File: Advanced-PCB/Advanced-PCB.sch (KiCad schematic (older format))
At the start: 150 parts, among them J1 USB_mini_micro_B, SW1 Esc, SW10 9, SW11 0, SW12 -, SW13 =, SW14 Back, SW15 `, SW2 1, SW3 2, SW4 3, SW5 4, SW6 5, SW7 6, SW8 7, SW9 8, U1 ATMEGA32U4, X1 16MHz

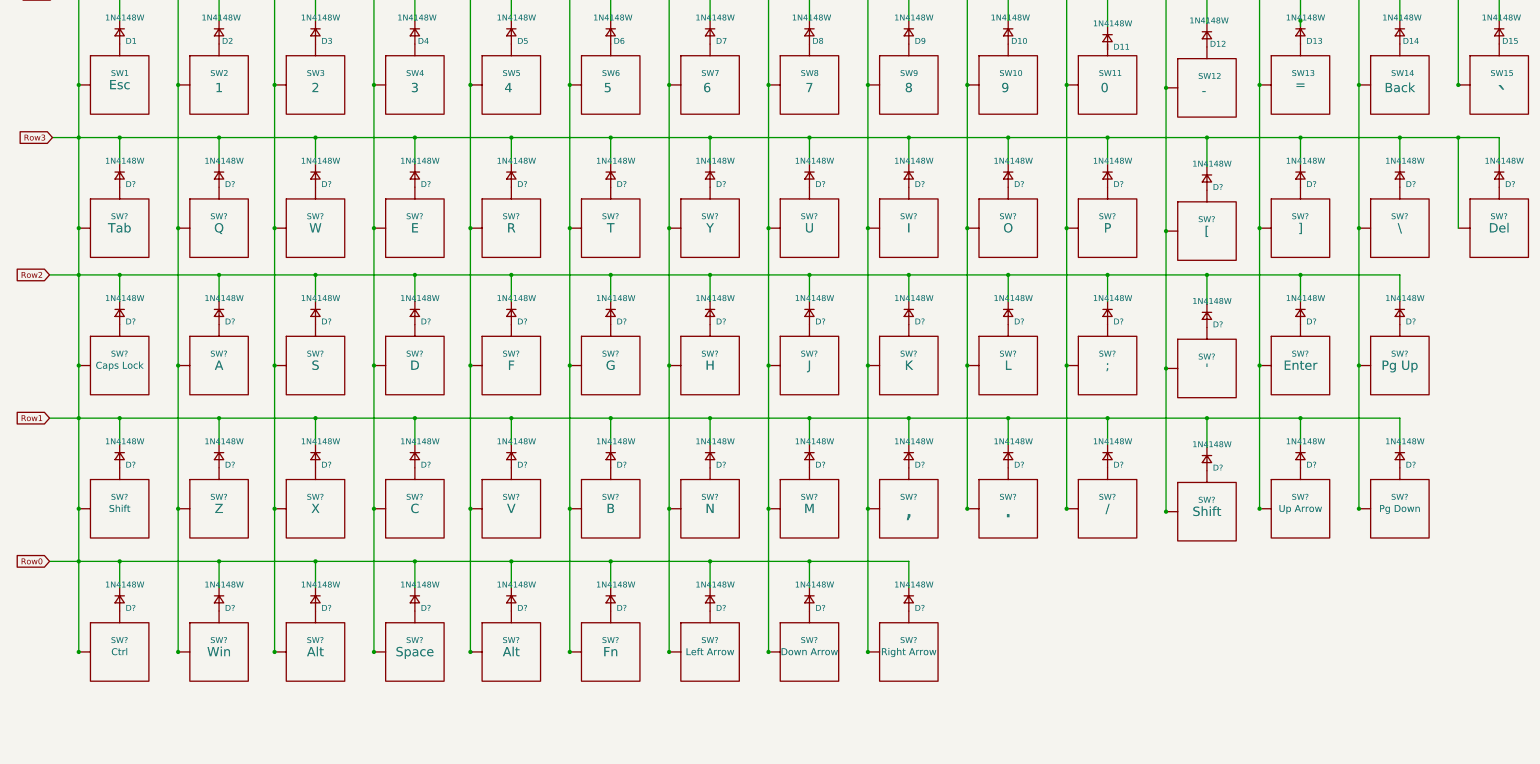
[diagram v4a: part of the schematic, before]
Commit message: Bottom Row Re-Alligned
Bottom Row Realigned to help with Trace in later steps.
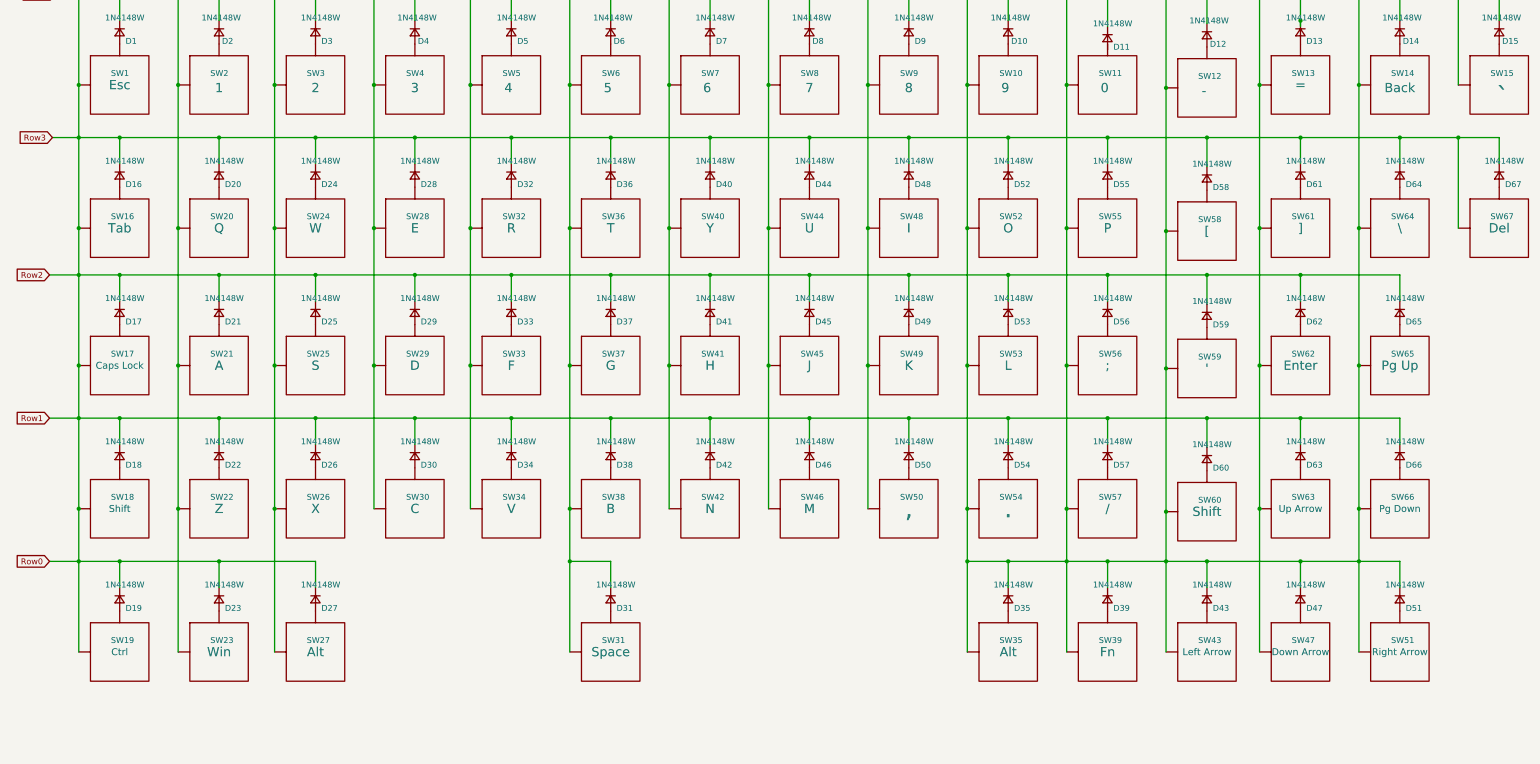
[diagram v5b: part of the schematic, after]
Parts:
- gave numbers to parts that had none: 104
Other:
- moved on the sheet: D31, D35, D39, D43, D47, D51, SW31, SW35, SW39, SW43, SW47, SW51

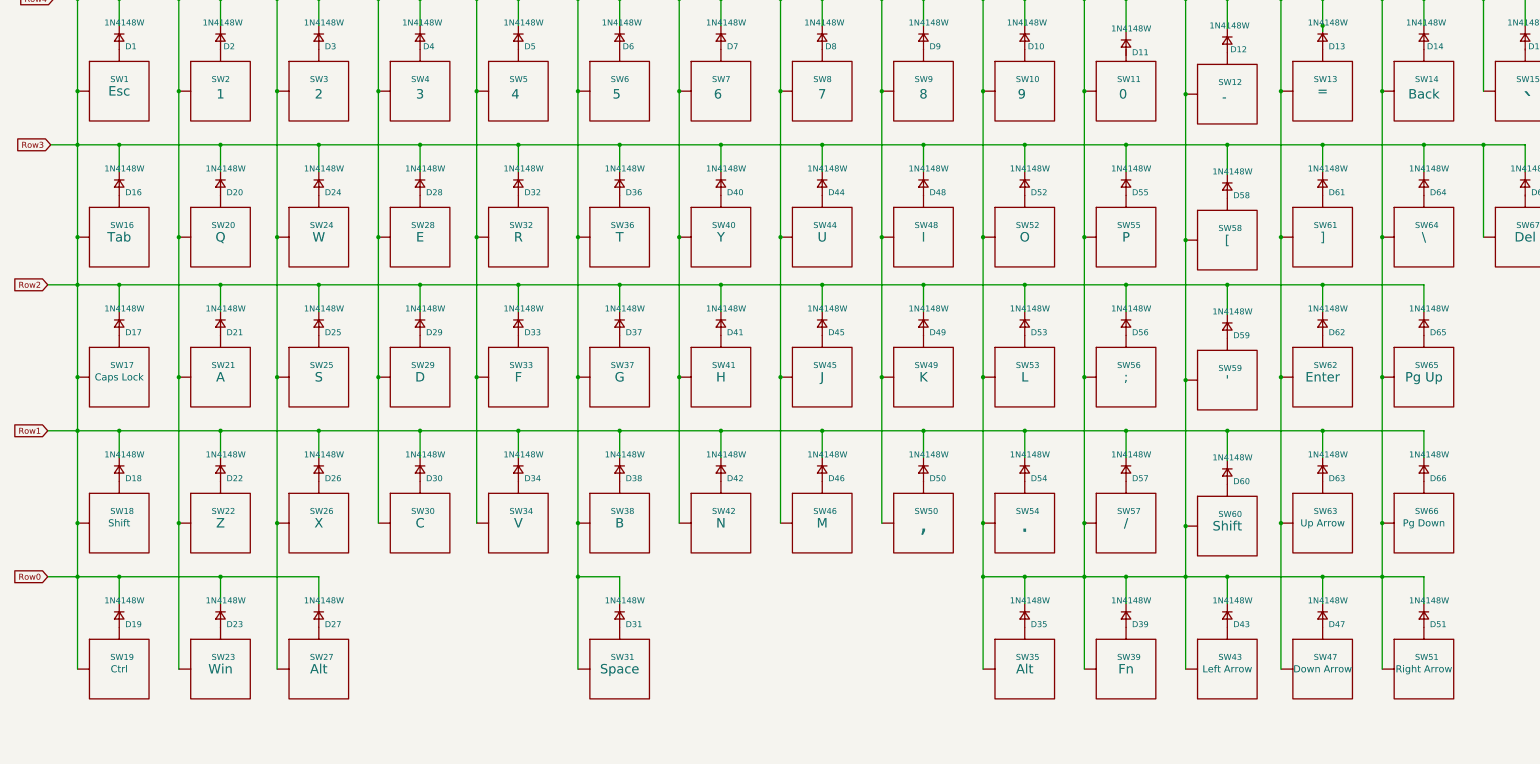
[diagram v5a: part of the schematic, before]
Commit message: KB Sizes Added
Non 1u switches sizes added to label.
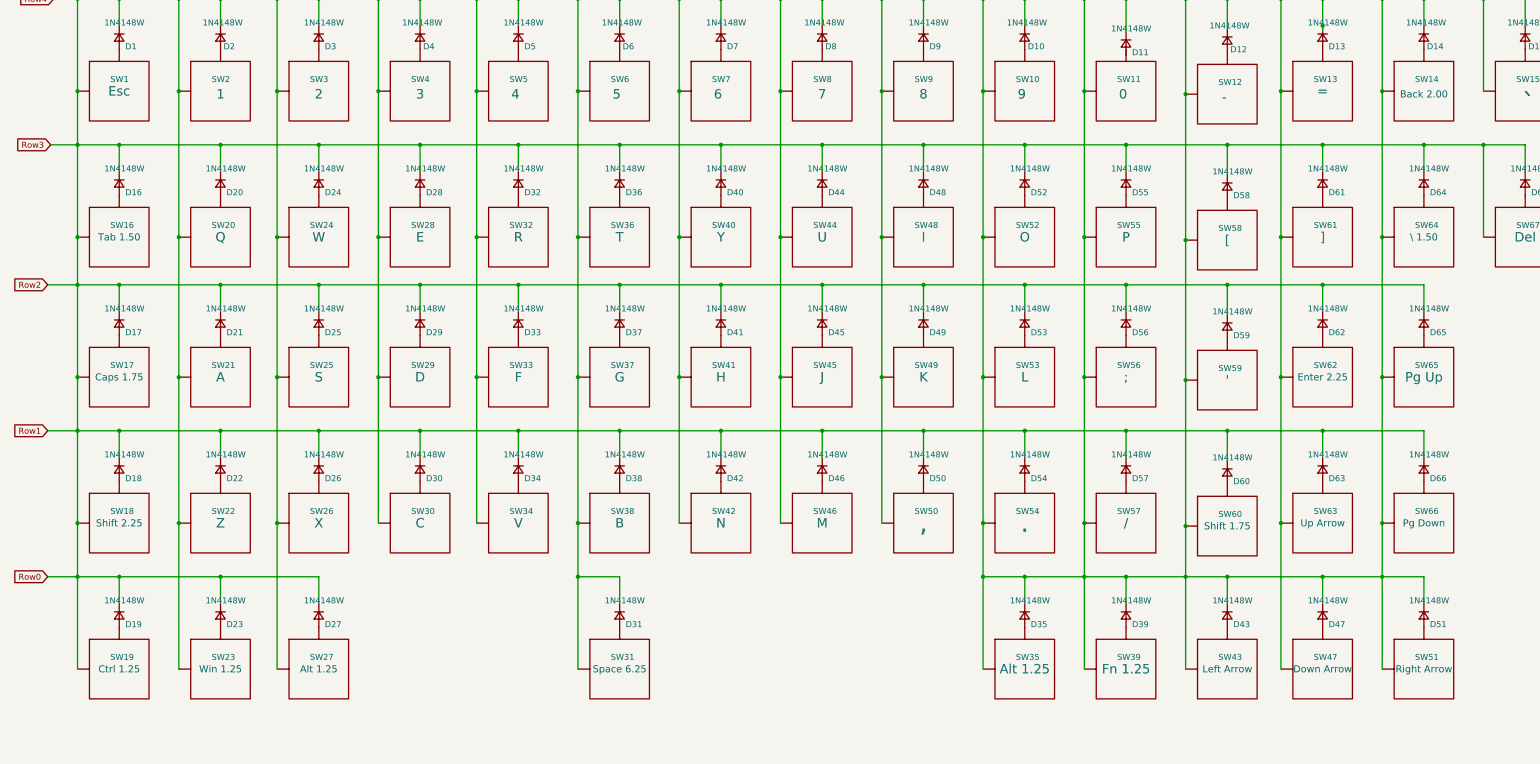
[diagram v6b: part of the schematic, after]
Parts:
- SW14: value Back -> Back 2.00
- SW16: value Tab -> Tab 1.50
- SW17: value Caps Lock -> Caps 1.75
- SW18: value Shift -> Shift 2.25
- SW19: value Ctrl -> Ctrl 1.25
- SW23: value Win -> Win 1.25
- SW27, SW35: value Alt -> Alt 1.25
- SW31: value Space -> Space 6.25
- SW39: value Fn -> Fn 1.25
- SW60: value Shift -> Shift 1.75
- SW62: value Enter -> Enter 2.25
- SW64: value \\ -> \\ 1.50
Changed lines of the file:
@@
 P 12550 1775
 F 0 "SW14" H 12475 1875 50  0000 L CNN
-F 1 "Back" H 12550 1750 79  0000 C CNN
+F 1 "Back 2.00" H 12550 1750 59  0000 C CNN
 F 2 "acheron_MXH:MX100H" H 12550 1775 50  0001 C CNN
 F 3 "" H 12550 1775 50  0001 C CNN
@@
 P 1600 3000
 F 0 "SW16" H 1525 3100 50  0000 L CNN
-F 1 "Tab" H 1600 3000 79  0000 C CNN
+F 1 "Tab 1.50" H 1600 3000 59  0000 C CNN
 F 2 "acheron_MXH:MX100H" H 1600 3000 50  0001 C CNN
 F 3 "" H 1600 3000 50  0001 C CNN
@@
 P 12550 3000
 F 0 "SW64" H 12475 3100 50  0000 L CNN
-F 1 "\\" H 12550 3000 79  0000 C CNN
+F 1 "\\ 1.50" H 12550 3000 59  0000 C CNN
 F 2 "acheron_MXH:MX100H" H 12550 3000 50  0001 C CNN
 F 3 "" H 12550 3000 50  0001 C CNN
@@
 P 1600 4175
 F 0 "SW17" H 1525 4275 50  0000 L CNN
-F 1 "Caps Lock" H 1600 4175 59  0000 C CNN
+F 1 "Caps 1.75" H 1600 4175 59  0000 C CNN
 F 2 "acheron_MXH:MX100H" H 1600 4175 50  0001 C CNN
 F 3 "" H 1600 4175 50  0001 C CNN
@@
 P 11700 4175
 F 0 "SW62" H 11625 4275 50  0000 L CNN
-F 1 "Enter" H 11700 4175 79  0000 C CNN
+F 1 "Enter 2.25" H 11700 4175 59  0000 C CNN
 F 2 "acheron_MXH:MX100H" H 11700 4175 50  0001 C CNN
 F 3 "" H 11700 4175 50  0001 C CNN
@@
 P 1600 5400
 F 0 "SW18" H 1525 5500 50  0000 L CNN
-F 1 "Shift" H 1600 5400 59  0000 C CNN
+F 1 "Shift 2.25" H 1600 5400 59  0000 C CNN
 F 2 "acheron_MXH:MX100H" H 1600 5400 50  0001 C CNN
 F 3 "" H 1600 5400 50  0001 C CNN
@@
 P 1600 6625
 F 0 "SW19" H 1525 6725 50  0000 L CNN
-F 1 "Ctrl" H 1600 6625 59  0000 C CNN
+F 1 "Ctrl 1.25" H 1600 6625 59  0000 C CNN
 F 2 "acheron_MXH:MX100H" H 1600 6625 50  0001 C CNN
 F 3 "" H 1600 6625 50  0001 C CNN
@@
 P 2450 6625
 F 0 "SW23" H 2375 6725 50  0000 L CNN
-F 1 "Win" H 2450 6625 79  0000 C CNN
+F 1 "Win 1.25" H 2450 6625 59  0000 C CNN
 F 2 "acheron_MXH:MX100H" H 2450 6625 50  0001 C CNN
 F 3 "" H 2450 6625 50  0001 C CNN
@@
 P 3275 6625
 F 0 "SW27" H 3200 6725 50  0000 L CNN
-F 1 "Alt" H 3275 6625 79  0000 C CNN
+F 1 "Alt 1.25" H 3275 6625 59  0000 C CNN
 F 2 "acheron_MXH:MX100H" H 3275 6625 50  0001 C CNN
 F 3 "" H 3275 6625 50  0001 C CNN
@@
 P 5800 6625
 F 0 "SW31" H 5725 6725 50  0000 L CNN
-F 1 "Space" H 5800 6625 79  0000 C CNN
+F 1 "Space 6.25" H 5800 6625 59  0000 C CNN
 F 2 "acheron_MXH:MX100H" H 5800 6625 50  0001 C CNN
 F 3 "" H 5800 6625 50  0001 C CNN
@@
 P 9200 6625
 F 0 "SW35" H 9125 6725 50  0000 L CNN
-F 1 "Alt" H 9200 6625 79  0000 C CNN
+F 1 "Alt 1.25" H 9200 6625 79  0000 C CNN
 F 2 "acheron_MXH:MX100H" H 9200 6625 50  0001 C CNN
 F 3 "" H 9200 6625 50  0001 C CNN
@@
 P 10050 6625
 F 0 "SW39" H 9975 6725 50  0000 L CNN
-F 1 "Fn" H 10050 6625 79  0000 C CNN
+F 1 "Fn 1.25" H 10050 6625 79  0000 C CNN
 F 2 "acheron_MXH:MX100H" H 10050 6625 50  0001 C CNN
 F 3 "" H 10050 6625 50  0001 C CNN
@@
 P 10900 5425
 F 0 "SW60" H 10825 5525 50  0000 L CNN
-F 1 "Shift" H 10900 5425 79  0000 C CNN
+F 1 "Shift 1.75" H 10900 5425 59  0000 C CNN
 F 2 "acheron_MXH:MX100H" H 10900 5425 50  0001 C CNN
 F 3 "" H 10900 5425 50  0001 C CNN

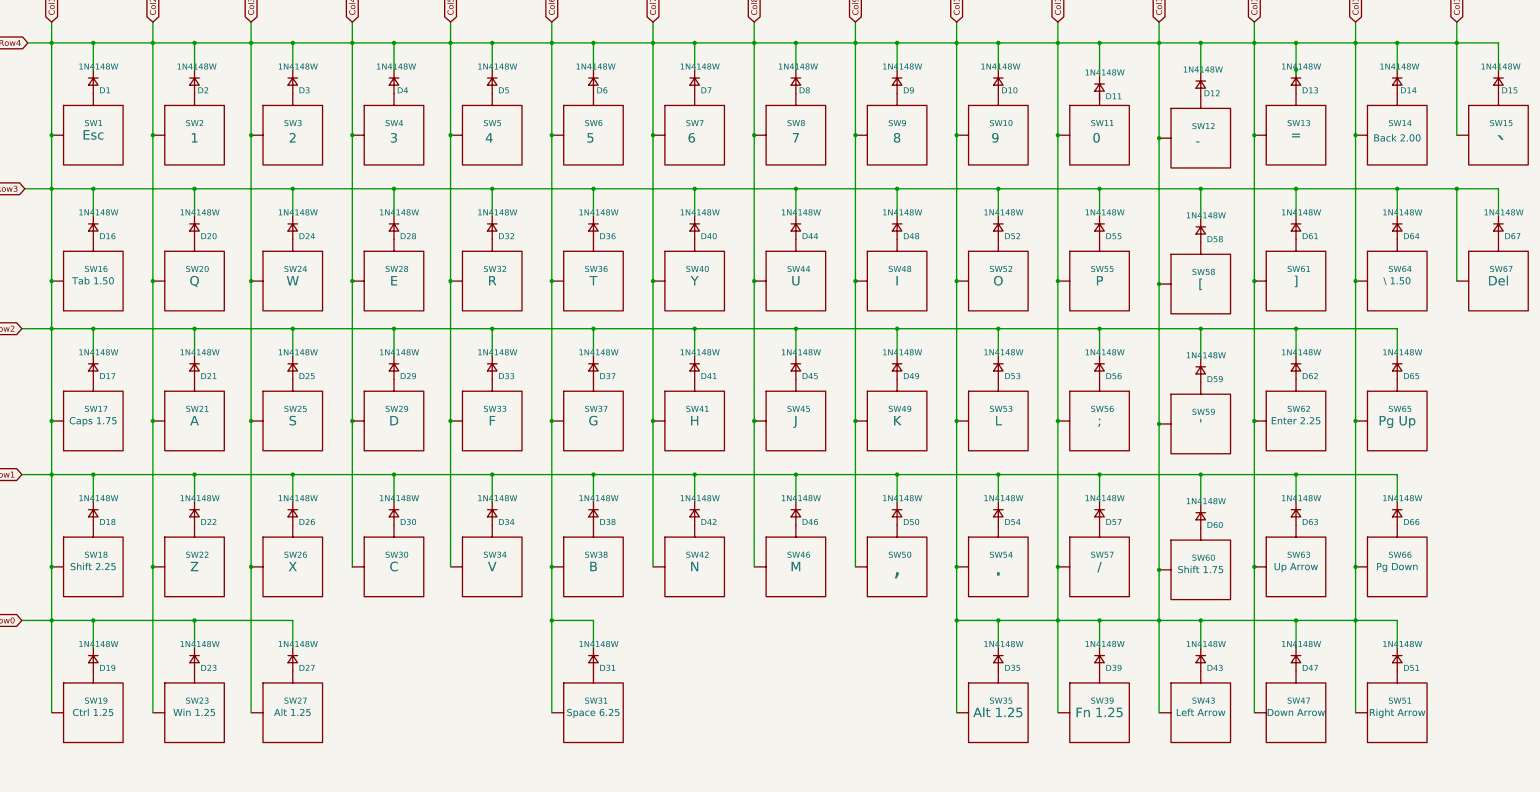
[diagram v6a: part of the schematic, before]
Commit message: Key Dimensions Corrected
All keys have the correct lenght and hot swap profile. Switches larger than 2u have north facing stabs.
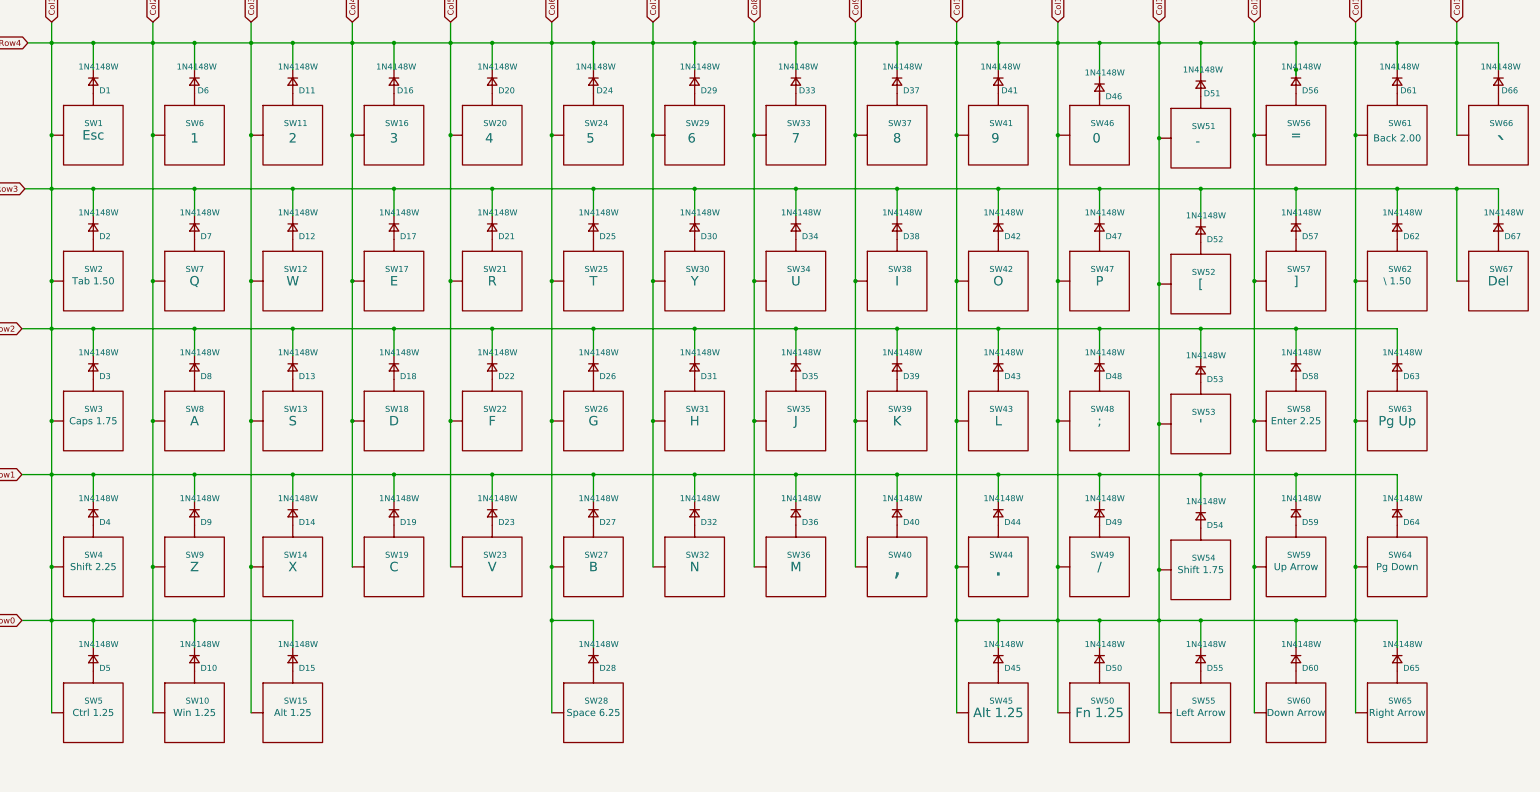
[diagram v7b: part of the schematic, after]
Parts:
- SW2: renamed from SW16; footprint acheron_MXH:MX100H -> acheron_MXH:MX150H
- SW28: renamed from SW31; footprint acheron_MXH:MX100H -> acheron_MXH:MX625HR
- SW3: renamed from SW17; footprint acheron_MXH:MX100H -> acheron_MXH:MX175H
- SW4: renamed from SW18; footprint acheron_MXH:MX100H -> acheron_MXH:MX225HR
- SW58: renamed from SW62; footprint acheron_MXH:MX100H -> acheron_MXH:MX225HR
- SW61: renamed from SW14; footprint acheron_MXH:MX100H -> acheron_MXH:MX200HR
- renumbered D23 to D10, D3 to D11, D24 to D12, D25 to D13, D26 to D14, D27 to D15, D4 to D16, D28 to D17, D29 to D18, D30 to D19, D16 to D2, D5 to D20, D32 to D21, D33 to D22, D34 to D23, D6 to D24, D36 to D25, D37 to D26, D38 to D27, D31 to D28, D7 to D29, D17 to D3, D40 to D30, D41 to D31, D42 to D32, D8 to D33, D44 to D34, D45 to D35, D46 to D36, D9 to D37, D48 to D38, D49 to D39, D18 to D4, D50 to D40, D10 to D41, D52 to D42, D53 to D43, D54 to D44, D35 to D45, D11 to D46, D55 to D47, D56 to D48, D57 to D49, D19 to D5, D39 to D50, D12 to D51, D58 to D52, D59 to D53, D60 to D54, D43 to D55, D13 to D56, D61 to D57, D62 to D58, D63 to D59, D2 to D6, D47 to D60, D14 to D61, D64 to D62, D65 to D63, D66 to D64, D51 to D65, D15 to D66, D20 to D7, D21 to D8, D22 to D9, SW23 to SW10, SW3 to SW11, SW24 to SW12, SW25 to SW13, SW26 to SW14, SW27 to SW15, SW4 to SW16, SW28 to SW17, SW29 to SW18, SW30 to SW19, SW5 to SW20, SW32 to SW21, SW33 to SW22, SW34 to SW23, SW6 to SW24, SW36 to SW25, SW37 to SW26, SW38 to SW27, SW7 to SW29, SW40 to SW30, SW41 to SW31, SW42 to SW32, SW8 to SW33, SW44 to SW34, SW45 to SW35, SW46 to SW36, SW9 to SW37, SW48 to SW38, SW49 to SW39, SW50 to SW40, SW10 to SW41, SW52 to SW42, SW53 to SW43, SW54 to SW44, SW35 to SW45, SW11 to SW46, SW55 to SW47, SW56 to SW48, SW57 to SW49, SW19 to SW5, SW39 to SW50, SW12 to SW51, SW58 to SW52, SW59 to SW53, SW60 to SW54, SW43 to SW55, SW13 to SW56, SW61 to SW57, SW63 to SW59, SW2 to SW6, SW47 to SW60, SW64 to SW62, SW65 to SW63, SW66 to SW64, SW51 to SW65, SW15 to SW66, SW20 to SW7, SW21 to SW8, SW22 to SW9

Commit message: PCB Layout Complete
Full PCB layed out in wanted order.
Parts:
- SW10, SW15, SW45, SW5, SW50: footprint acheron_MXH:MX100H -> acheron_MXH:MX125H
- SW54: footprint acheron_MXH:MX100H -> acheron_MXH:MX175H
- SW62: footprint acheron_MXH:MX100H -> acheron_MXH:MX150H
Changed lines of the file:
@@
 F 0 "SW62" H 12475 3100 50  0000 L CNN
 F 1 "\\ 1.50" H 12550 3000 59  0000 C CNN
-F 2 "acheron_MXH:MX100H" H 12550 3000 50  0001 C CNN
+F 2 "acheron_MXH:MX150H" H 12550 3000 50  0001 C CNN
 F 3 "" H 12550 3000 50  0001 C CNN
 	1    12550 3000
@@
 F 0 "SW5" H 1525 6725 50  0000 L CNN
 F 1 "Ctrl 1.25" H 1600 6625 59  0000 C CNN
-F 2 "acheron_MXH:MX100H" H 1600 6625 50  0001 C CNN
+F 2 "acheron_MXH:MX125H" H 1600 6625 50  0001 C CNN
 F 3 "" H 1600 6625 50  0001 C CNN
 	1    1600 6625
@@
 F 0 "SW10" H 2375 6725 50  0000 L CNN
 F 1 "Win 1.25" H 2450 6625 59  0000 C CNN
-F 2 "acheron_MXH:MX100H" H 2450 6625 50  0001 C CNN
+F 2 "acheron_MXH:MX125H" H 2450 6625 50  0001 C CNN
 F 3 "" H 2450 6625 50  0001 C CNN
 	1    2450 6625
@@
 F 0 "SW15" H 3200 6725 50  0000 L CNN
 F 1 "Alt 1.25" H 3275 6625 59  0000 C CNN
-F 2 "acheron_MXH:MX100H" H 3275 6625 50  0001 C CNN
+F 2 "acheron_MXH:MX125H" H 3275 6625 50  0001 C CNN
 F 3 "" H 3275 6625 50  0001 C CNN
 	1    3275 6625
@@
 F 0 "SW45" H 9125 6725 50  0000 L CNN
 F 1 "Alt 1.25" H 9200 6625 79  0000 C CNN
-F 2 "acheron_MXH:MX100H" H 9200 6625 50  0001 C CNN
+F 2 "acheron_MXH:MX125H" H 9200 6625 50  0001 C CNN
 F 3 "" H 9200 6625 50  0001 C CNN
 	1    9200 6625
@@
 F 0 "SW50" H 9975 6725 50  0000 L CNN
 F 1 "Fn 1.25" H 10050 6625 79  0000 C CNN
-F 2 "acheron_MXH:MX100H" H 10050 6625 50  0001 C CNN
+F 2 "acheron_MXH:MX125H" H 10050 6625 50  0001 C CNN
 F 3 "" H 10050 6625 50  0001 C CNN
 	1    10050 6625
@@
 F 0 "SW54" H 10825 5525 50  0000 L CNN
 F 1 "Shift 1.75" H 10900 5425 59  0000 C CNN
-F 2 "acheron_MXH:MX100H" H 10900 5425 50  0001 C CNN
+F 2 "acheron_MXH:MX175H" H 10900 5425 50  0001 C CNN
 F 3 "" H 10900 5425 50  0001 C CNN
 	1    10900 5425
